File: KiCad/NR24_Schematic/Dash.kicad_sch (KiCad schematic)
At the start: 9 parts, among them SW1 TI power switch, SW2 Shifter Switch, SW5 Key Switch, SW6 12V E-stop

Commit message: v6
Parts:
- added J9: AVR-TPI-6, symbol NR24_Car:AVR-TPI-6
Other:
- note removed: "Display Screen"
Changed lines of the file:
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@@
     (stroke (width 0) (type default))
-  )
-  (polyline (pts (xy 153.67 78.74) (xy 161.29 78.74))
-    (stroke (width 0.5) (type solid))
   )
   (wire (pts (xy 195.58 106.68) (xy 198.12 106.68))
     (stroke (width 0) (type default))
   )
-  (polyline (pts (xy 161.29 78.74) (xy 161.29 90.17))
-    (stroke (width 0.5) (type solid))
-  )
   (wire (pts (xy 110.49 72.39) (xy 114.3 72.39))
     (stroke (width 0) (type default))
@@
     (stroke (width 0) (type default))
   )
-  (polyline (pts (xy 153.67 78.74) (xy 153.67 90.17))
-    (stroke (width 0.5) (type solid))
-  )
   (bus (pts (xy 157.48 90.17) (xy 157.48 106.68))
     (stroke (width 0) (type default))
@@
     (stroke (width 0) (type default))
   )
-  (polyline (pts (xy 161.29 90.17) (xy 153.67 90.17))
-    (stroke (width 0.5) (type solid))
-  )
-  (text "|\\--/|\n| o_o |\n \\_ ^_/" (at 153.67 90.17 0)
-    (effects (font (size 1.27 1.27)) (justify left bottom))
-  )
-  (text "Display\nScreen\n" (at 153.67 83.82 0)
-    (effects (font (size 1.27 1.27)) (justify left bottom))
+  (text "|\\--/|\n| o_o |\n \\_ ^_/" (at 162.56 46.99 0)
+    (effects (font (size 3 3)) (justify left bottom))
   )
   (text "Dash CAN" (at 152.4 76.2 0)
@@
         )
       )
+    )
+  )
+  (symbol (lib_id "NR24_Car:AVR-TPI-6") (at 222.25 36.83 0) (unit 1)
+    (in_bom yes) (on_board yes) (dnp no) (fields_autoplaced)
+    (property "Reference" "J9" (at 217.805 24.13 0)
+      (effects (font (size 1.27 1.27)))
+    )
+    (property "Value" "AVR-TPI-6" (at 217.805 26.67 0)
+      (effects (font (size 1.27 1.27)))
+    )
+    (property "Footprint" "" (at 215.9 38.1 90)
+      (effects (font (size 1.27 1.27)) hide)
+    )
+    (property "Datasheet" " ~" (at 189.865 50.8 0)
+      (effects (font (size 1.27 1.27)) hide)
+    )
+    (pin "1")
+    (pin "1")
+    (pin "2")
+    (pin "2")
+    (pin "3")
+    (pin "3")
+    (pin "4")
+    (pin "4")
+    (pin "5")
+    (pin "5")
+    (pin "6")
+    (pin "6")
+    (instances
+      (project "Car_TractiveSystem_v2"
+        (path "/588b5c14-1813-4e1d-9dbe-940839ecebe3/62b4fa84-4530-4bff-bc03-eb6ea850cb52"
+          (reference "J9") (unit 1)
+        )
+      )

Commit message: B-? where are stops connected to
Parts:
- added LA2: IMD Safety Light, symbol Device:Lamp
- J9: value AVR-TPI-6 -> AEM Dash
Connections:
- net Dash +12V is gone; now on net 12V Power: SW1.1 (A), SW6.2 (B)
- net GND is gone; now on net 12V GND to TI: LA1.1 (-), LA3.1 (-)
- net N_Light(+): now also LA5.1 (-); no longer LA5.2 (+)
- net N_Light(-): now also LA5.2 (+); no longer LA5.1 (-)
- net 12V Power: now reaches J9.1 (12V_Battery+)
- net 12V GND to TI: now reaches J9.2 (Battery-)
- new net Dash Error +: LA2.2 (+)
- new net Dash Error -: LA2.1 (-)
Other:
- note removed: "Dash CAN"
- moved on the sheet: LA2, LA3, LA4, SW2, SW5, SW6

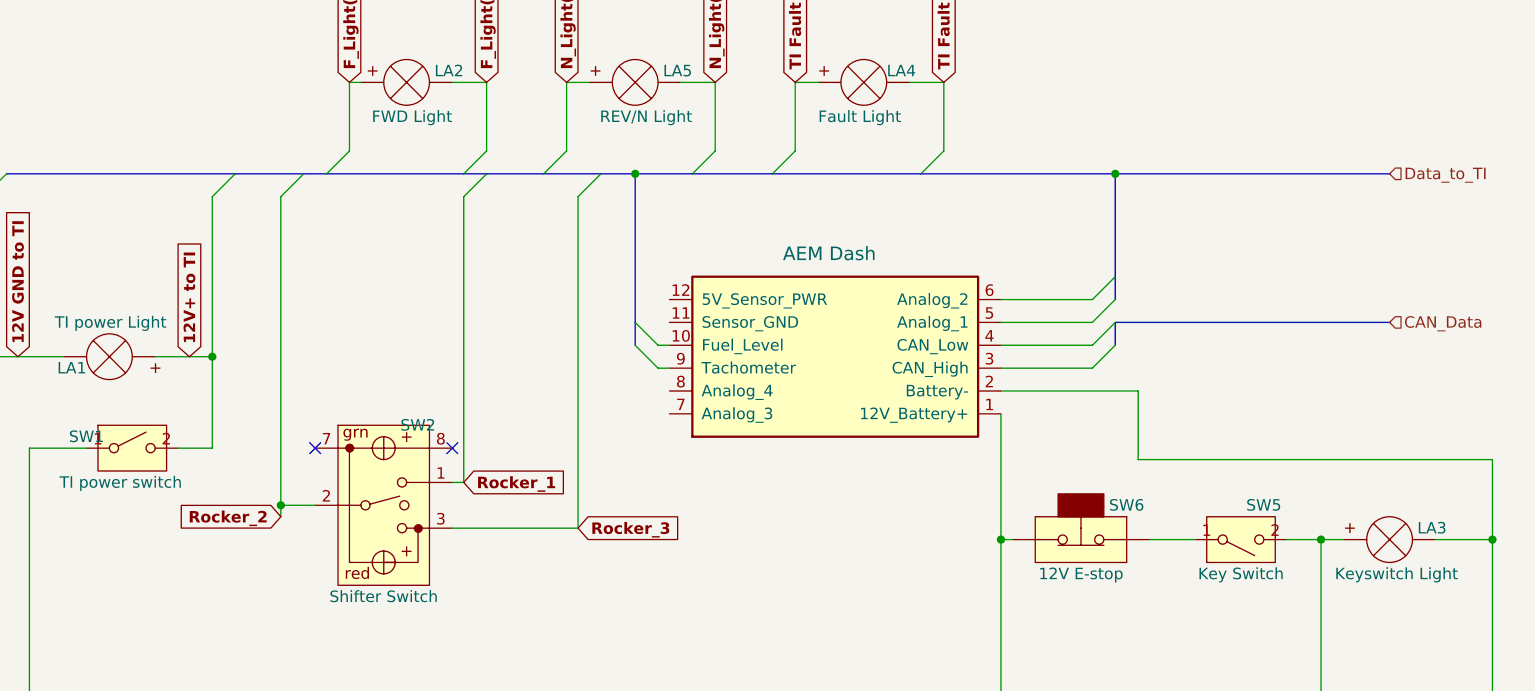
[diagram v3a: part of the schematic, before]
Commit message: Almost there
Finish the key switch terminal, and the TI board schematic.
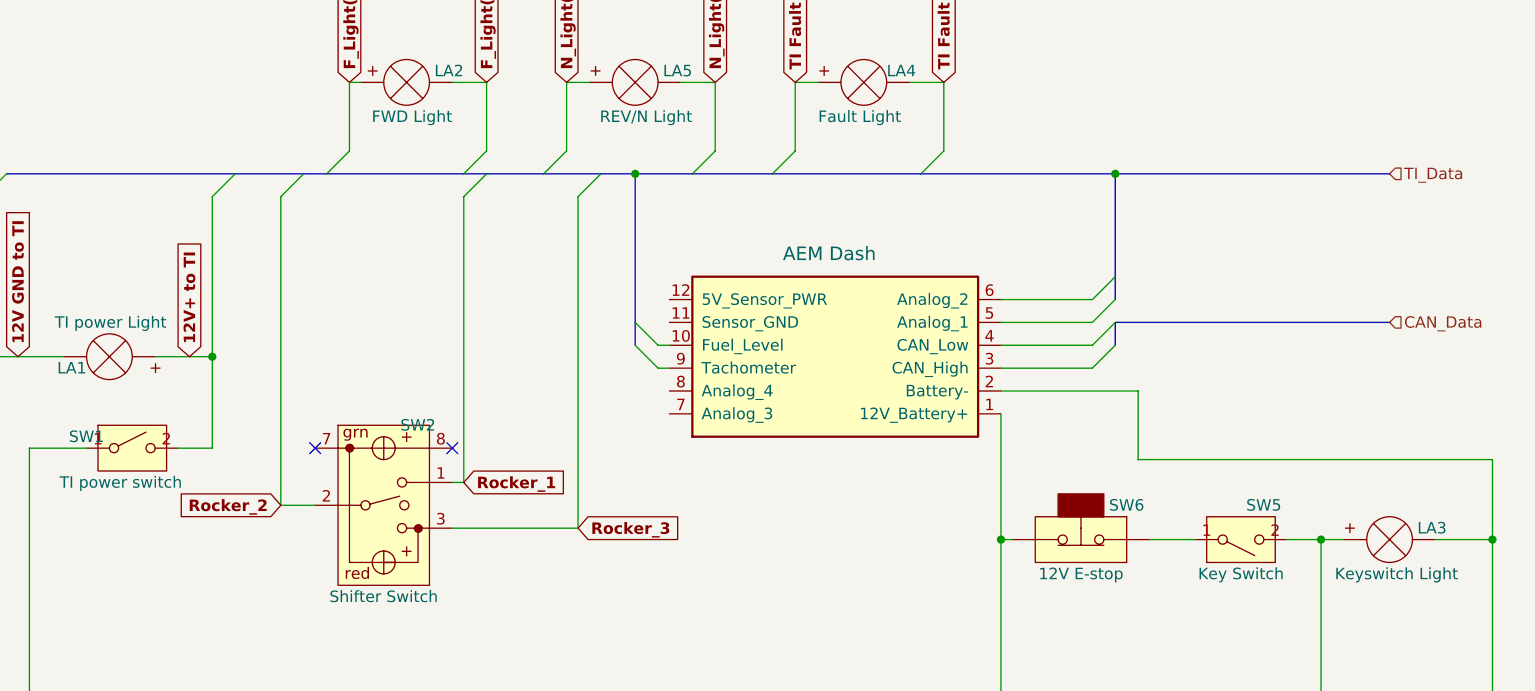
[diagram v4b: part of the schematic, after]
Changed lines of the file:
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@@
   (junction (at 187.96 102.87) (diameter 0) (color 0 0 0 0)
-  )
-  (junction (at 107.95 99.06) (diameter 0) (color 0 0 0 0)
   )
   (junction (at 100.33 82.55) (diameter 0) (color 0 0 0 0)
@@
   )
   (wire (pts (xy 127 101.6) (xy 140.97 101.6))
-    (stroke (width 0) (type default))
-  )
-  (wire (pts (xy 107.95 99.06) (xy 107.95 100.33))
     (stroke (width 0) (type default))
   )
@@
     )
   )
-  (global_label "Rocker_2" (shape input) (at 107.95 100.33 180) (fields_autoplaced)
+  (global_label "Rocker_2" (shape input) (at 107.95 99.06 180) (fields_autoplaced)
     (effects (font (size 1.27 1.27) (thickness 0.254) bold) (justify right))
-    (property "Intersheetrefs" "${INTERSHEET_REFS}" (at 96.7589 100.203 0)
+    (property "Intersheetrefs" "${INTERSHEET_REFS}" (at 96.7589 98.933 0)
       (effects (font (size 1.27 1.27) (thickness 0.254) bold) (justify right) hide)
     )
@@
     (effects (font (size 1.27 1.27)) (justify right))
   )
-  (hierarchical_label "Data_to_TI" (shape input) (at 231.14 62.23 0) (fields_autoplaced)
+  (hierarchical_label "TI_Data" (shape input) (at 231.14 62.23 0) (fields_autoplaced)
     (effects (font (size 1.27 1.27)) (justify left))
   )
